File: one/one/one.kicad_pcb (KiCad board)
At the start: 4 copper layers, 57 x 65 mm, 67 parts, among them J101 Conn_01x04_Pin, J102 Conn_01x04_Pin, J103 ADC, J104 DAC, J105 SJ-252X, J106 Conn_01x04_Pin, J107 Conn_01x04_Pin, J108 Conn_02x04_Counter_Clockwise, J109 Conn_01x04_Pin, J110 Conn_01x05_Pin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

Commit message: add footprints
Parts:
- added G***: LOGO, logo:hats-logo-5mm, F.Cu at (148.2, 127.7)
- J105, J113: footprint rpi:SJ-252X -> hats:SJ-252X
- J501: footprint rpi:CUI-PJ-018 -> hats:CUI-PJ-018
- Q1001: footprint rpi:TSOT-23-5-mirrored -> hats:TSOT-23-5-mirrored
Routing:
- net /ADC/MISO: track 43.2 -> 41.3 mm
- net /DAC/CH_{C}: track 12.0 -> 11.2 mm
- net /ADC/SCK: track 43.6 -> 42.9 mm
- net GND: vias 169 -> 196
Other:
- board text added: "${TITLE} ${REVISION} ${ISSUE_DATE} ${LINK}"
- board text removed: "${TITLE} ${REVISION} ${ISSUE_DATE}"

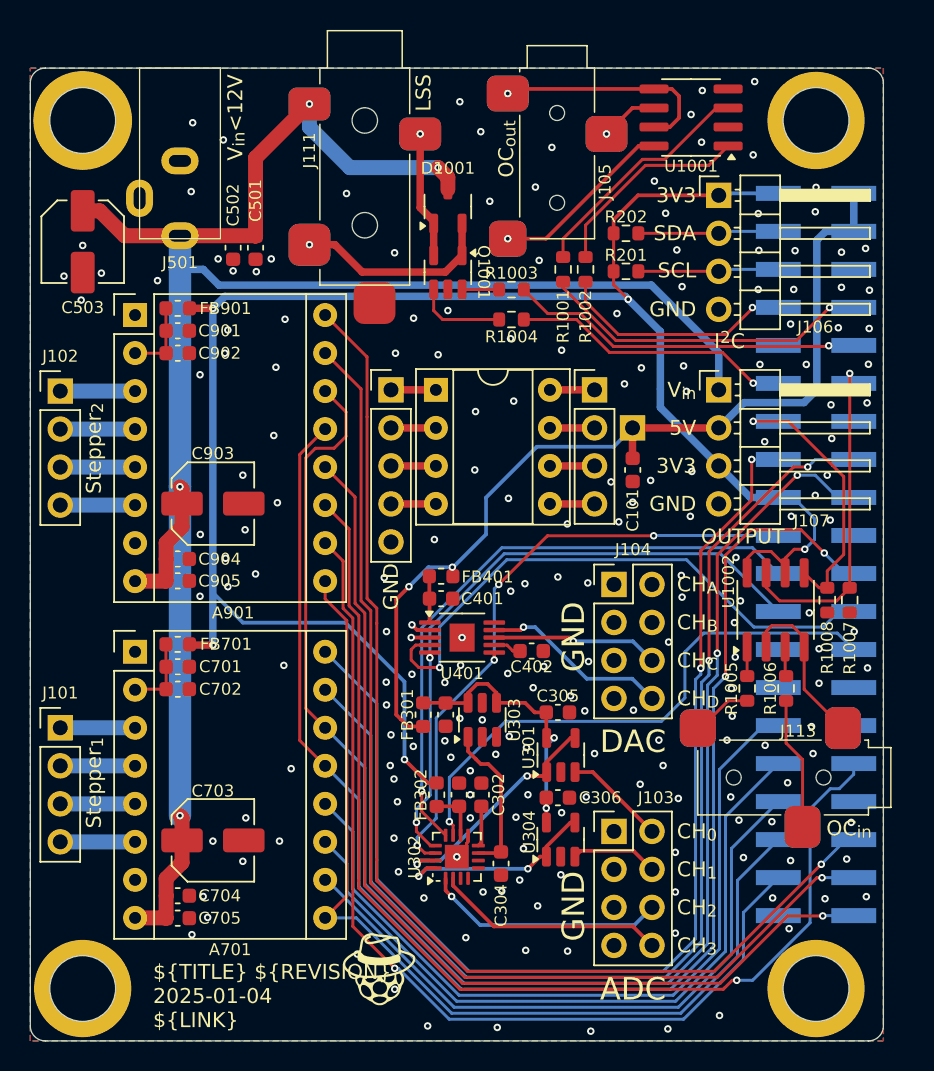
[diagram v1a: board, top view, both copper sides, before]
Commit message: add EEPROM, remove one mounting hole
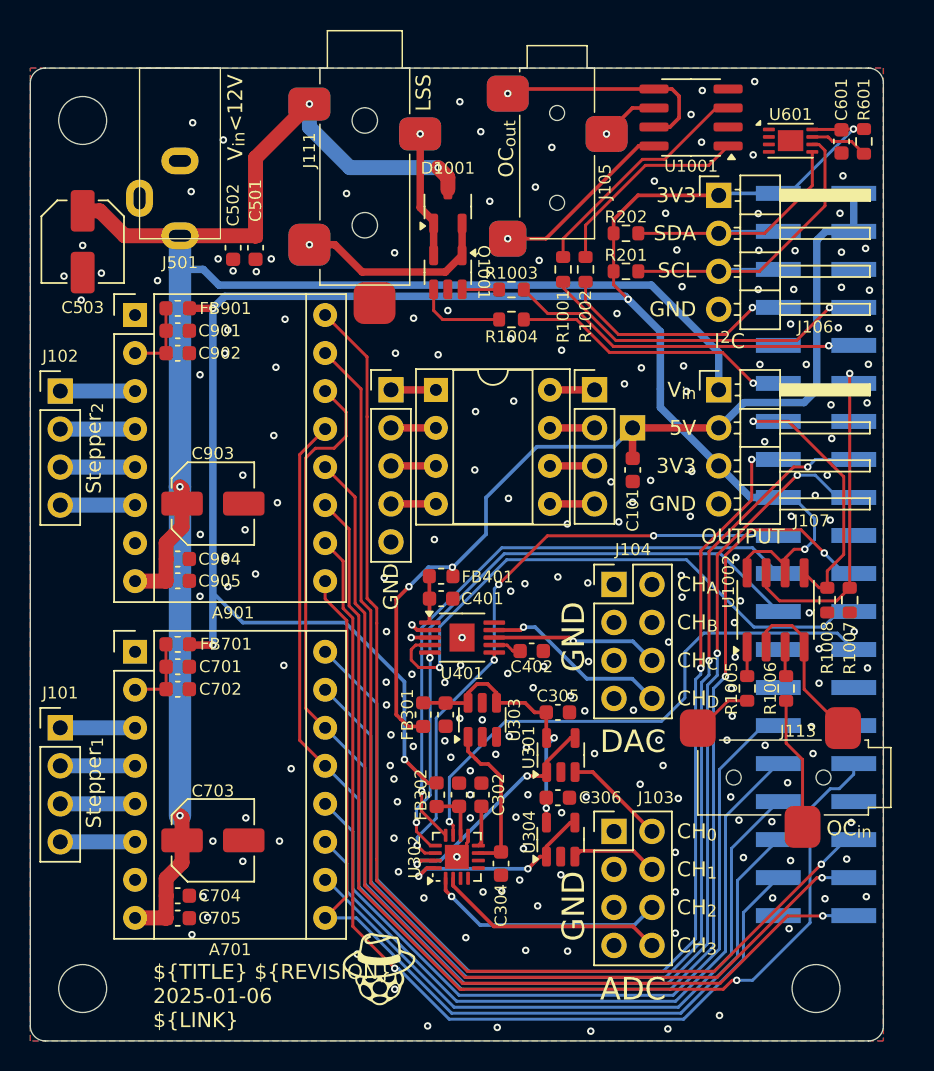
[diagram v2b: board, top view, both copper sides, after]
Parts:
- removed H802: M3, Mounting_Wuerth:Mounting_Wuerth_WA-SMSI-M3_H1mm_9774010360
- added C601: 100nF, Capacitor_SMD:C_0603_1608Metric, F.Cu at (179.2, 72.4)
- added R601: 1k, Resistor_SMD:R_0603_1608Metric, F.Cu at (180.7, 72.4)
- added U601: 24LC512, Package_DFN_QFN:DFN-8-1EP_3x2mm_P0.5mm_EP1.7x1.4mm, F.Cu at (175.8, 72.3)
- H801, H803, H804: footprint Mounting_Wuerth:Mounting_Wuerth_WA-SMSI-M3_H1mm_9774010360 -> MountingHole:MountingHole_3.2mm_M3_DIN965
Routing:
- net /EEPROM/SCL: track 9.41 -> 23.0 mm
- net +3V3: track 126.0 -> 136.3 mm, vias 5 -> 6
- net /EEPROM/SDA: track 9.41 -> 19.2 mm
- net Net-(U601-WP): track 0.00 -> 3.92 mm
